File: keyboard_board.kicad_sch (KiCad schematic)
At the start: 16 parts, among them J1 Conn_02x20_Odd_Even, J2 Trackpad Connector, J3 Rp500KB, J4 S3B-PH-SM4-TB, J5 S3B-PH-SM4-TB, P1 S2B-PH-SM4-TB, P2 S2B-PH-SM4-TB, P4 S2B-PH-SM4-TB, SW1 Reset, U1 SC0915, U2 74HC165, U3 74HC165

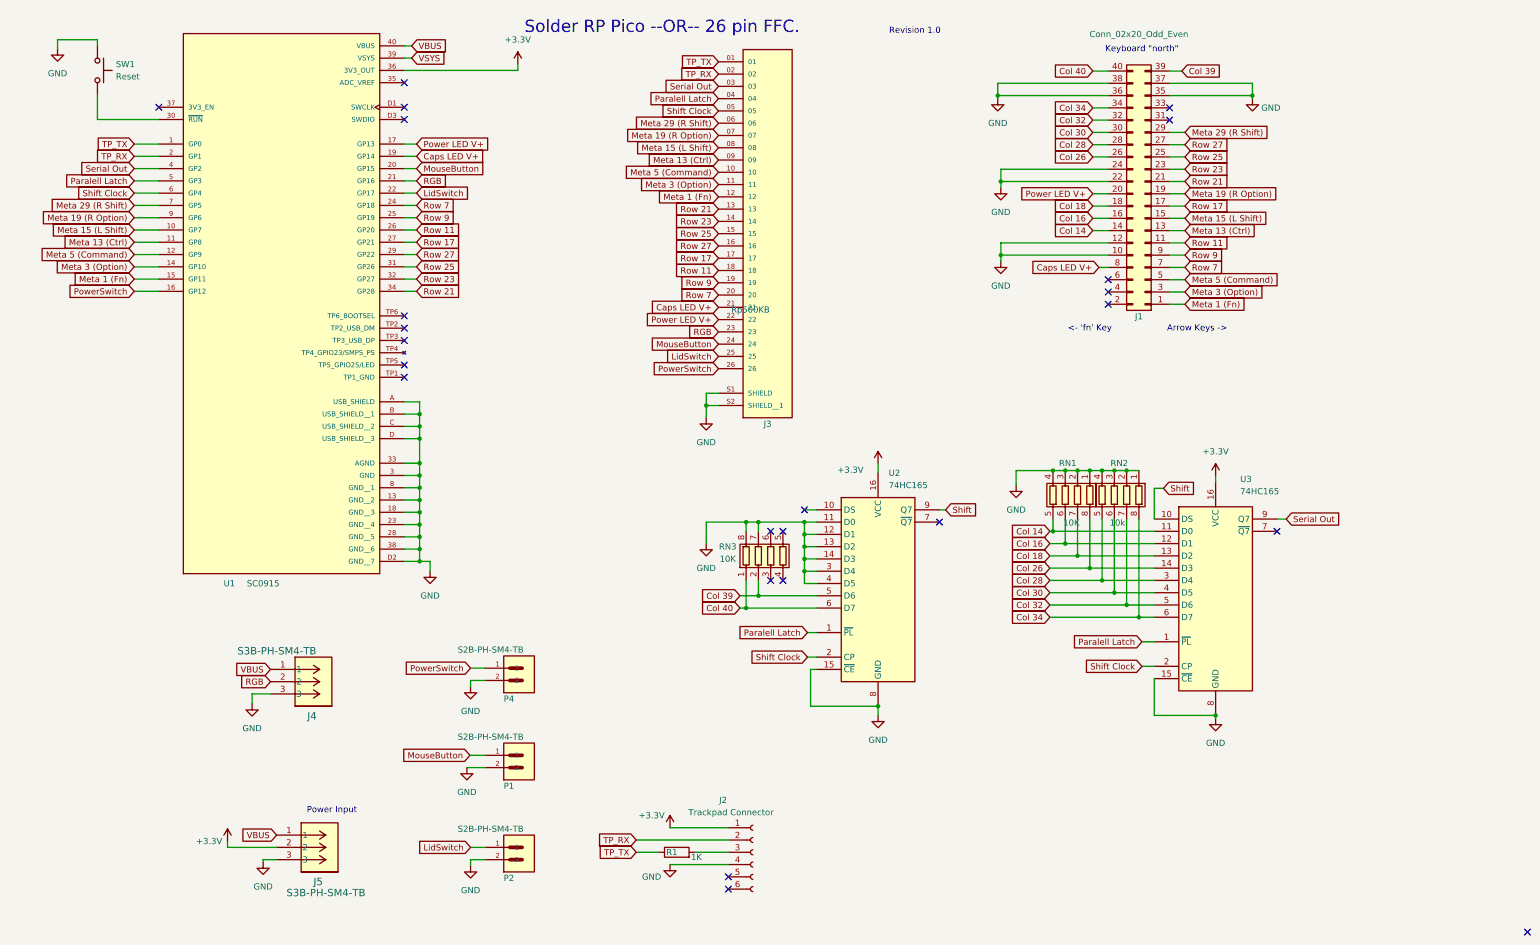
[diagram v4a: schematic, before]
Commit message: Reworks Pico-based into discrete components
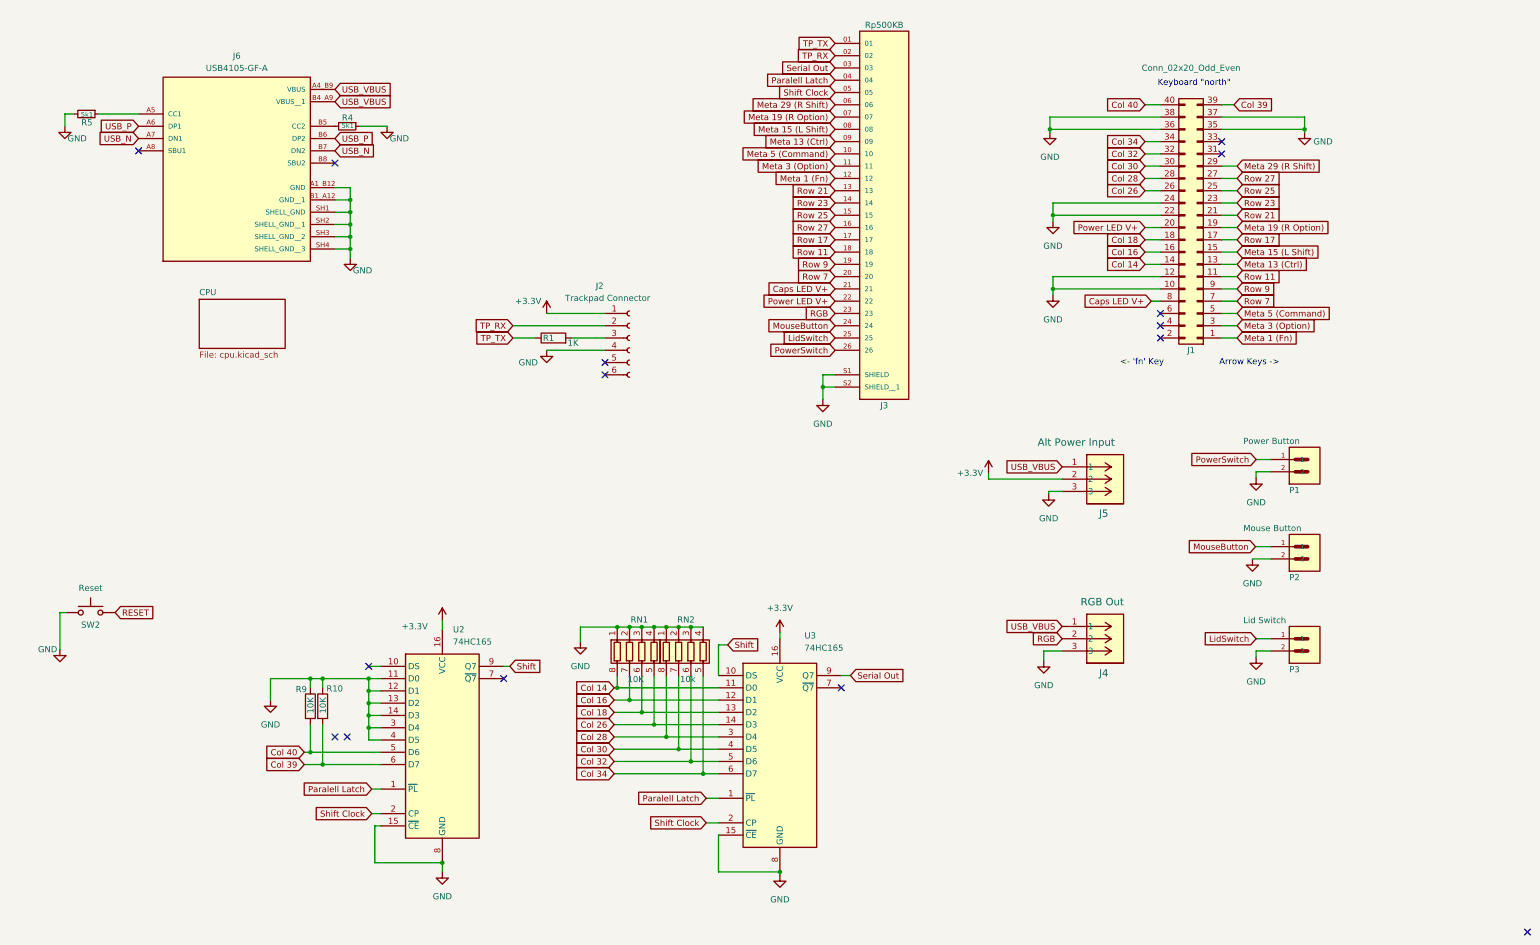
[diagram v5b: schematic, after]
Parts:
- removed P4: S2B-PH-SM4-TB, Aaron:JST_S2B-PH-SM4-TB, symbol Aaron:S2B-PH-SM4-TB
- removed RN3: 10K, Resistor_SMD:R_Array_Convex_4x1206, symbol Device:R_Pack04
- removed SW1: Reset, Aaron:SW4_PTS815 SJM 250 SMTR LFS_CNK, symbol Switch:SW_Push
- removed U1: SC0915, SC0915:MODULE_SC0915, symbol SC0915:SC0915
- added J6: USB4105-GF-A, Aaron:GCT_USB4105-GF-A, symbol USB4105-GF-A:USB4105-GF-A
- added P3: Lid Switch, Aaron:JST_S2B-PH-SM4-TB, symbol Aaron:S2B-PH-SM4-TB
- added R10, R9: 10K, Resistor_SMD:R_0805_2012Metric, symbol Device:R
- added R4, R5: 5k1, Resistor_SMD:R_0805_2012Metric, symbol Device:R_Small
- added SW2: Reset, Aaron:SW4_PTS815 SJM 250 SMTR LFS_CNK, symbol Switch:SW_Push
- J4: value S3B-PH-SM4-TB -> RGB Out
- J5: value S3B-PH-SM4-TB -> Alt Power Input
- P1: value S2B-PH-SM4-TB -> Power Button
- P2: value S2B-PH-SM4-TB -> Mouse Button
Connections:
- net Col 14: now also RN1.8 (R1.2); no longer RN1.5 (R4.2)
- net Col 16: now also RN1.7 (R2.2); no longer RN1.6 (R3.2)
- net Col 18: now also RN1.6 (R3.2); no longer RN1.7 (R2.2)
- net Col 26: now also RN1.5 (R4.2); no longer RN1.8 (R1.2)
- net Col 28: now also RN2.8 (R1.2); no longer RN2.5 (R4.2)
- net Col 30: now also RN2.7 (R2.2); no longer RN2.6 (R3.2)
- net Col 32: now also RN2.6 (R3.2); no longer RN2.7 (R2.2)
- net Col 34: now also RN2.5 (R4.2); no longer RN2.8 (R1.2)
- net Col 39: now also U2.6 (D7), R10.2; no longer U2.5 (D6)
- net Col 40: now also U2.5 (D6), R9.2; no longer U2.6 (D7)
- net GND: now also J6.A1_B12 (GND), J6.B1_A12 (GND__1), J6.SH1 (SHELL_GND), J6.SH2 (SHELL_GND__1), J6.SH3 (SHELL_GND__2), J6.SH4 (SHELL_GND__3), P3.2, R10.1, R4.1, R5.2, R9.1, SW2.1
- net LidSwitch: now also P3.1; no longer P2.1
- net MouseButton : now also P2.1; no longer P1.1
- net PowerSwitch: now also P1.1
- net VBUS renamed USB_VBUS
- net USB_VBUS: now also J6.A4_B9 (VBUS), J6.B4_A9 (VBUS__1)
- new net: J6.B5 (CC2), R4.2
- new net: J6.A5 (CC1), R5.1
- new net RESET: SW2.2
- new net USB_N: J6.A7 (DN1), J6.B7 (DN2)
- new net USB_P: J6.A6 (DP1), J6.B6 (DP2)
- no-connect marks 24 -> 15
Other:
- added sheet CPU (cpu.kicad_sch)
- note removed: "Power Input"
- note removed: "Revision ${REVISION}"
- note removed: "Solder RP Pico --OR-- 26 pin FFC."
- moved on the sheet: RN1, RN2, U2, U3

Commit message: prod version, I think
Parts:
- removed J3: Rp500KB, Aaron:AMPHENOL_10051922-2610ELF, symbol 10051922-2610ELF:10051922-2610ELF
- removed J5: Alt Power Input, Aaron:CONN3_S3B-PH_JST, symbol Aaron:S3B-PH-SM4-TB
- removed SW2: Reset, Aaron:SW4_PTS815 SJM 250 SMTR LFS_CNK, symbol Switch:SW_Push
- R4, R5: footprint Resistor_SMD:R_0805_2012Metric -> Resistor_SMD:R_0603_1608Metric
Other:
- note added: "Connectors"
- moved on the sheet: J1, J2, J4, J6, P1, P2, P3, R1, R10, R4, R5, R9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
